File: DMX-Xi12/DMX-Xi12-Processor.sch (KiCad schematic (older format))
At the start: 3 parts, among them U1 LPC11U68JBD100E

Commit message: added output stage
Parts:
- added R? (x4): 10K, symbol R
- added SW?: DIPS_04, symbol DIPS_04
- added SW?: SW_PUSH, symbol SW_PUSH
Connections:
- net +5V: now also R?.1, R?.1, R?.1, R?.1
- net GND: now also SW?.1, SW?.2, SW?.2, SW?.3, SW?.4
- net at U1.1 (PIO2_23): now also R?.2, SW?.8
- net RX: now reaches U1.17 (PIO0_20)
- net RX_ENABLE: now reaches U1.33 (PIO0_21)
- net TX_ENABLE: now reaches U1.62 (PIO0_22)
- net at U1.75 (PIO2_20): now also R?.2, SW?.5
- net at U1.76 (PIO2_21): now also R?.2, SW?.6
- net at U1.77 (PIO2_22): now also R?.2, SW?.7
- net at C?.1, R?.2, U1.8 (RESET/PIO0_0): now also SW?.1
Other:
- moved on the sheet: R?
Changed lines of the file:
@@
 LIBS:valves
 LIBS:DMX-Xi12
+LIBS:dips-s
+LIBS:MyPower
 LIBS:DMX-Xi12-cache
 EELAYER 25 0
@@
 $Descr A4 11693 8268
 encoding utf-8
-Sheet 3 3
+Sheet 3 10
 Title "DMX-Xi12 Processor"
 Date ""
@@
 	1    0    0    -1
 $EndComp
-Wire Wire Line
-	5600 1750 5600 1700
-Wire Wire Line
-	5400 1700 6200 1700
-Wire Wire Line
-	5700 1700 5700 1750
-Wire Wire Line
-	5800 1700 5800 1750
-Connection ~ 5700 1700
-Wire Wire Line
-	5900 1700 5900 1750
-Connection ~ 5800 1700
-Wire Wire Line
-	6000 1700 6000 1750
-Connection ~ 5900 1700
-Wire Wire Line
-	6100 1700 6100 1750
-Connection ~ 6000 1700
-Wire Wire Line
-	6200 1700 6200 1750
-Connection ~ 6100 1700
-Wire Wire Line
-	6300 1400 6300 1750
-Wire Wire Line
-	6300 1700 6800 1700
-Wire Wire Line
-	6400 1700 6400 1750
-Wire Wire Line
-	6500 1700 6500 1750
-Connection ~ 6400 1700
-Wire Wire Line
-	6600 1700 6600 1750
-Connection ~ 6500 1700
-Wire Wire Line
-	6700 1700 6700 1750
-Connection ~ 6600 1700
-Wire Wire Line
-	6800 1700 6800 1750
-Connection ~ 6700 1700
-Wire Wire Line
-	5400 1400 5400 1750
-Connection ~ 5600 1700
-Wire Wire Line
-	5500 1750 5500 1600
-Wire Wire Line
-	5500 1600 6300 1600
-Connection ~ 6300 1700
 NoConn ~ 4900 1750
 $Comp
@@
 	1    0    0    -1
 $EndComp
-Connection ~ 6300 1600
 $Comp
 L GND #PWR?
@@
 	-1   0    0    1
 $EndComp
-Connection ~ 5400 1700
 $Comp
 L +5V #PWR?
 U 1 1 56AFFF45
-P 8100 2200
-F 0 "#PWR?" H 8100 2050 50  0001 C CNN
-F 1 "+5V" H 8100 2340 50  0000 C CNN
-F 2 "" H 8100 2200 50  0000 C CNN
-F 3 "" H 8100 2200 50  0000 C CNN
-	1    8100 2200
+P 8100 2050
+F 0 "#PWR?" H 8100 1900 50  0001 C CNN
+F 1 "+5V" H 8100 2190 50  0000 C CNN
+F 2 "" H 8100 2050 50  0000 C CNN
+F 3 "" H 8100 2050 50  0000 C CNN
+	1    8100 2050
 	1    0    0    -1
 $EndComp
@@
 L R R?
 U 1 1 56AFFF7D
-P 8100 2400
-F 0 "R?" V 8180 2400 50  0000 C CNN
-F 1 "4K7" V 8100 2400 50  0000 C CNN
-F 2 "" V 8030 2400 50  0000 C CNN
-F 3 "" H 8100 2400 50  0000 C CNN
-	1    8100 2400
+P 8100 2300
+F 0 "R?" V 8180 2300 50  0000 C CNN
+F 1 "4K7" V 8100 2300 50  0000 C CNN
+F 2 "" V 8030 2300 50  0000 C CNN
+F 3 "" H 8100 2300 50  0000 C CNN
+	1    8100 2300
 	1    0    0    -1
 $EndComp
@@
 	1    0    0    -1
 $EndComp
-Wire Wire Line
-	8100 2200 8100 2250
-Wire Wire Line
-	8100 2550 8100 2650
-Wire Wire Line
-	8100 2950 8100 3000
-Wire Wire Line
-	8100 2600 7850 2600
-Connection ~ 8100 2600
 Text HLabel 4500 5950 3    60   Output ~ 0
 CH3
@@
 Text HLabel 7400 5950 3    60   Output ~ 0
 CH32
+$Comp
+L DIPS_04 SW?
+U 1 1 56B54085
+P 3300 5250
+F 0 "SW?" V 3050 5250 60  0000 C CNN
+F 1 "DIPS_04" V 3550 5250 60  0000 C CNN
+F 2 "" H 3300 5250 60  0000 C CNN
+F 3 "" H 3300 5250 60  0000 C CNN
+	1    3300 5250
+	1    0    0    -1
+$EndComp
+$Comp
+L R R?
+U 1 1 56B54160
+P 3100 4300
+F 0 "R?" V 3180 4300 50  0000 C CNN
+F 1 "10K" V 3100 4300 50  0000 C CNN
+F 2 "" V 3030 4300 50  0000 C CNN
+F 3 "" H 3100 4300 50  0000 C CNN
+	1    3100 4300
+	1    0    0    -1
+$EndComp
+$Comp
+L R R?
+U 1 1 56B541AC
+P 3200 4300
+F 0 "R?" V 3280 4300 50  0000 C CNN
+F 1 "10K" V 3200 4300 50  0000 C CNN
+F 2 "" V 3130 4300 50  0000 C CNN
+F 3 "" H 3200 4300 50  0000 C CNN
+	1    3200 4300
+	1    0    0    -1
+$EndComp
+$Comp
+L R R?
+U 1 1 56B541F0
+P 3300 4300
+F 0 "R?" V 3380 4300 50  0000 C CNN
+F 1 "10K" V 3300 4300 50  0000 C CNN
+F 2 "" V 3230 4300 50  0000 C CNN
+F 3 "" H 3300 4300 50  0000 C CNN
+	1    3300 4300
+	1    0    0    -1
+$EndComp
+$Comp
+L R R?
+U 1 1 56B5422B
+P 3400 4300
+F 0 "R?" V 3480 4300 50  0000 C CNN
+F 1 "10K" V 3400 4300 50  0000 C CNN
+F 2 "" V 3330 4300 50  0000 C CNN
+F 3 "" H 3400 4300 50  0000 C CNN
+	1    3400 4300
+	1    0    0    -1
+$EndComp
+$Comp
+L +5V #PWR?
+U 1 1 56B54680
+P 3250 3900
+F 0 "#PWR?" H 3250 3750 50  0001 C CNN
+F 1 "+5V" H 3250 4040 50  0000 C CNN
+F 2 "" H 3250 3900 50  0000 C CNN
+F 3 "" H 3250 3900 50  0000 C CNN
+	1    3250 3900
+	1    0    0    -1
+$EndComp
+Text HLabel 8150 4600 2    60   Input ~ 0
+RX
+Text HLabel 8150 4700 2    60   Output ~ 0
+RX_ENABLE
+Text HLabel 8150 4800 2    60   Output ~ 0
+TX_ENABLE
+$Comp
+L GND #PWR?
+U 1 1 56B5699D
+P 3300 5750
+F 0 "#PWR?" H 3300 5500 50  0001 C CNN
+F 1 "GND" H 3300 5600 50  0000 C CNN
+F 2 "" H 3300 5750 50  0000 C CNN
+F 3 "" H 3300 5750 50  0000 C CNN
+	1    3300 5750
+	1    0    0    -1
+$EndComp
+$Comp
+L SW_PUSH SW?
+U 1 1 56B572F2
+P 8450 2900
+F 0 "SW?" H 8600 3010 50  0000 C CNN
+F 1 "SW_PUSH" H 8450 2820 50  0000 C CNN
+F 2 "" H 8450 2900 50  0000 C CNN
+F 3 "" H 8450 2900 50  0000 C CNN
+	1    8450 2900
+	0    1    1    0
+$EndComp
+Wire Wire Line
+	5600 1750 5600 1700
+Wire Wire Line
+	5400 1700 6200 1700
+Wire Wire Line
+	5700 1700 5700 1750
+Wire Wire Line
+	5800 1700 5800 1750
+Connection ~ 5700 1700
+Wire Wire Line
+	5900 1700 5900 1750
+Connection ~ 5800 1700
+Wire Wire Line
+	6000 1700 6000 1750
+Connection ~ 5900 1700
+Wire Wire Line
+	6100 1700 6100 1750
+Connection ~ 6000 1700
+Wire Wire Line
+	6200 1700 6200 1750
+Connection ~ 6100 1700
+Wire Wire Line
+	6300 1400 6300 1750
+Wire Wire Line
+	6300 1700 6800 1700
+Wire Wire Line
+	6400 1700 6400 1750
+Wire Wire Line
+	6500 1700 6500 1750
+Connection ~ 6400 1700
+Wire Wire Line
+	6600 1700 6600 1750
+Connection ~ 6500 1700
+Wire Wire Line
+	6700 1700 6700 1750
+Connection ~ 6600 1700
+Wire Wire Line
+	6800 1700 6800 1750
+Connection ~ 6700 1700
+Wire Wire Line
+	5400 1400 5400 1750
+Connection ~ 5600 1700
+Wire Wire Line
+	5500 1750 5500 1600
+Wire Wire Line
+	5500 1600 6300 1600
+Connection ~ 6300 1700
+Connection ~ 6300 1600
+Connection ~ 5400 1700
+Wire Wire Line
+	8100 2450 8100 2650
+Wire Wire Line
+	8100 2950 8100 3000
+Wire Wire Line
+	8100 2600 7850 2600
+Connection ~ 8100 2600
 Wire Wire Line
 	4300 5750 4300 5950
@@
 Wire Wire Line
 	7400 5750 7400 5950
+Wire Wire Line
+	3100 4450 3100 4900
+Wire Wire Line
+	3200 4450 3200 4800
+Wire Wire Line
+	3300 4450 3300 4700
+Wire Wire Line
+	3400 4600 3400 4450
+Wire Wire Line
+	3100 4150 3400 4150
+Connection ~ 3200 4150
+Connection ~ 3300 4150
+Wire Wire Line
+	3250 4150 3250 3900
+Connection ~ 3250 4150
+Wire Wire Line
+	8150 4600 7850 4600
+Wire Wire Line
+	7850 4700 8150 4700
+Wire Wire Line
+	8150 4800 7850 4800
+Wire Wire Line
+	3150 5050 3150 4900
+Connection ~ 3150 4900
+Wire Wire Line
+	3250 5050 3250 4800
+Connection ~ 3250 4800
+Wire Wire Line
+	3350 5050 3350 4700
+Connection ~ 3350 4700
+Wire Wire Line
+	3450 5050 3450 4600
+Connection ~ 3450 4600
+Wire Wire Line
+	3150 5450 3150 5550
+Wire Wire Line
+	3150 5550 3450 5550
+Wire Wire Line
+	3300 5550 3300 5750
+Wire Wire Line
+	3450 5550 3450 5450
+Connection ~ 3300 5550
+Wire Wire Line
+	3350 5450 3350 5550
+Connection ~ 3350 5550
+Wire Wire Line
+	3250 5450 3250 5550
+Connection ~ 3250 5550
+Wire Wire Line
+	3400 4600 3850 4600
+Wire Wire Line
+	3300 4700 3850 4700
+Wire Wire Line
+	3200 4800 3850 4800
+Wire Wire Line
+	3100 4900 3850 4900
+Wire Wire Line
+	8100 2050 8100 2150
+Wire Wire Line
+	8450 2600 8450 2500
+Wire Wire Line
+	8450 2500 8100 2500
+Connection ~ 8100 2500
+$Comp
+L GND #PWR?
+U 1 1 56B57753
+P 8450 3300
+F 0 "#PWR?" H 8450 3050 50  0001 C CNN
+F 1 "GND" H 8450 3150 50  0000 C CNN
+F 2 "" H 8450 3300 50  0000 C CNN
+F 3 "" H 8450 3300 50  0000 C CNN
+	1    8450 3300
+	1    0    0    -1
+$EndComp
+Wire Wire Line
+	8450 3300 8450 3200
 $EndSCHEMATC

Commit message: more schematic
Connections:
- net Zero_crossing: now reaches U1.57 (PIO2_19)
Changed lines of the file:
@@
 Wire Wire Line
 	8450 3300 8450 3200
+Text HLabel 3500 3600 0    60   Output ~ 0
+Zero_crossing
+Wire Wire Line
+	3500 3600 3600 3600
+Wire Wire Line
+	3600 3600 3600 4500
+Wire Wire Line
+	3600 4500 3850 4500
 $EndSCHEMATC

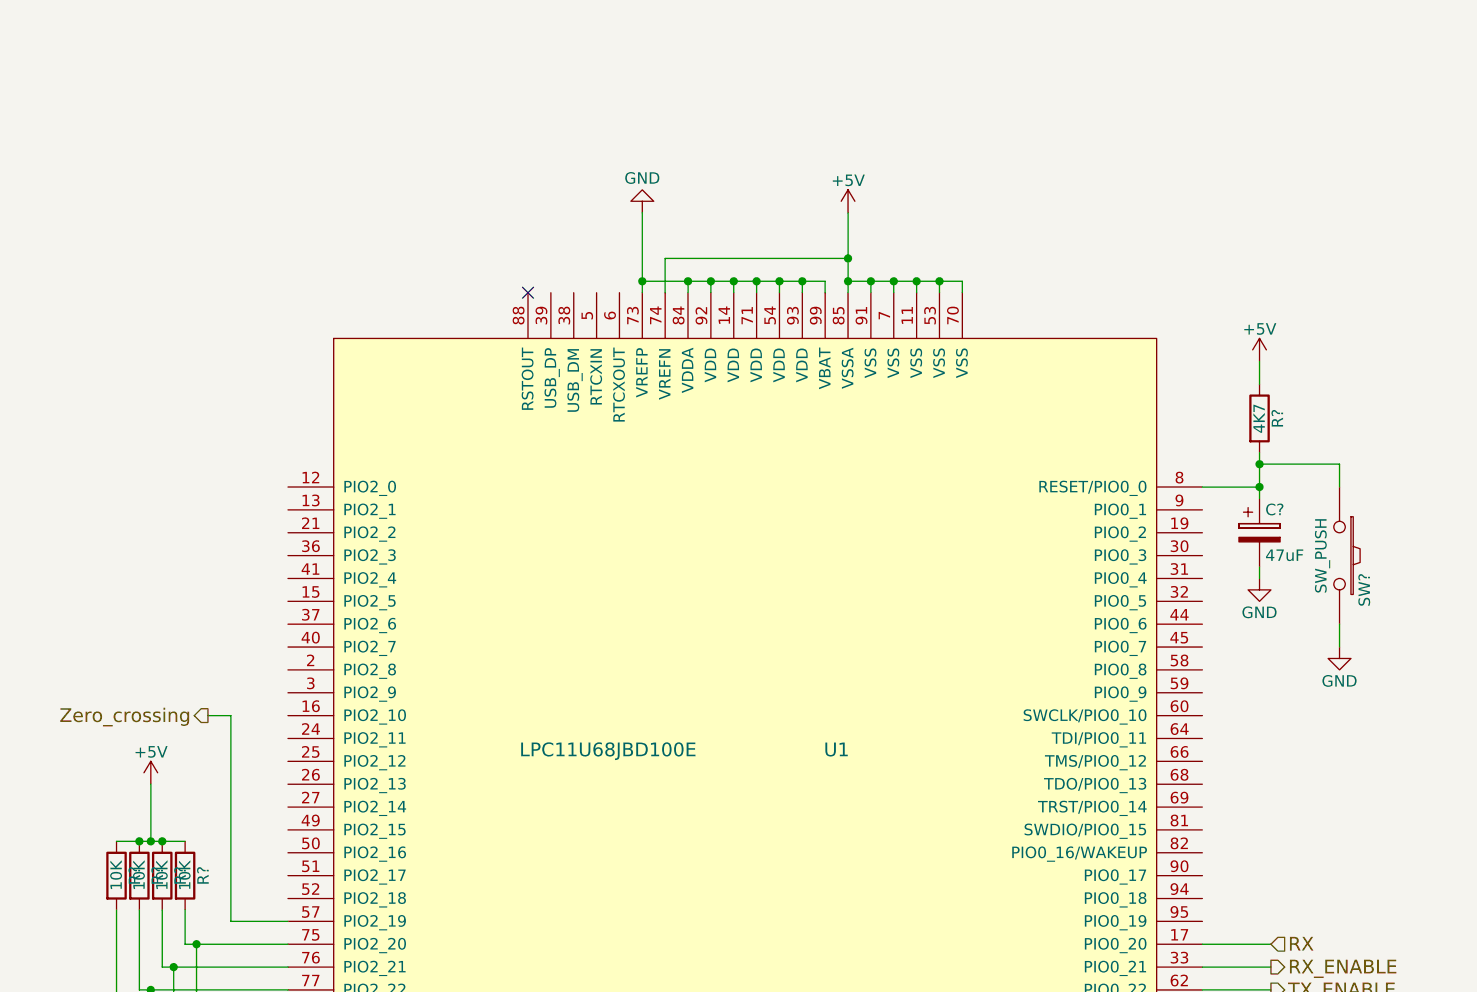
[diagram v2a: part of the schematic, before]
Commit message: changed processor to 3.3v and added programming
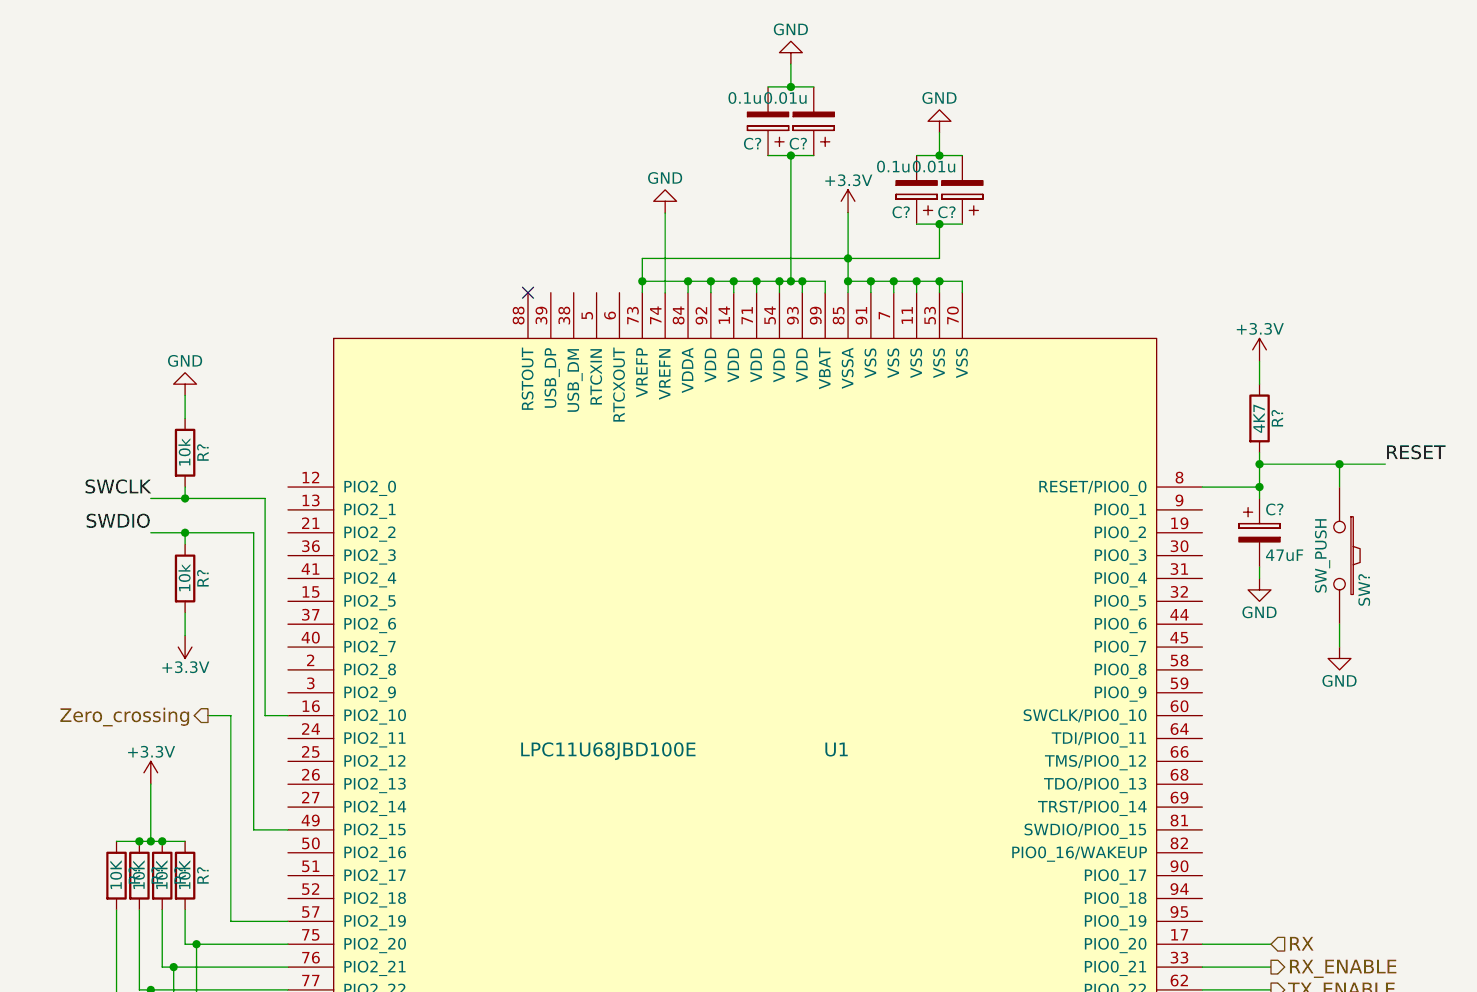
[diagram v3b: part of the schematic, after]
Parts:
- added C? (x2): 0.1u, symbol CP
- added C? (x2): 0.01u, symbol CP
- added R? (x2): 10k, symbol R
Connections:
- net GND: now also U1.74 (VREFN), C?.2, C?.2, C?.2, C?.2, R?.1; no longer U1.14 (VDD), U1.54 (VDD), U1.71 (VDD), U1.73 (VREFP), U1.84 (VDDA), U1.92 (VDD), U1.93 (VDD), U1.99 (VBAT)
- net SWCLK: now reaches U1.16 (PIO2_10)
- net SWCLK: now also R?.2
- net SWDIO: now reaches U1.49 (PIO2_15)
- net SWDIO: now also R?.1
- net RESET: now reaches C?.1, R?.2, SW?.1, U1.8 (RESET/PIO0_0)
- net +5V renamed +3V3
- net +3V3: now also U1.14 (VDD), U1.54 (VDD), U1.71 (VDD), U1.73 (VREFP), U1.84 (VDDA), U1.92 (VDD), U1.93 (VDD), U1.99 (VBAT), C?.1, C?.1, C?.1, C?.1, R?.2; no longer U1.74 (VREFN)
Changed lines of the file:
@@
 NoConn ~ 4900 1750
 $Comp
-L +5V #PWR?
-U 1 1 56AFFDE3
-P 6300 1400
-F 0 "#PWR?" H 6300 1250 50  0001 C CNN
-F 1 "+5V" H 6300 1540 50  0000 C CNN
-F 2 "" H 6300 1400 50  0000 C CNN
-F 3 "" H 6300 1400 50  0000 C CNN
-	1    6300 1400
-	1    0    0    -1
-$EndComp
-$Comp
 L GND #PWR?
 U 1 1 56AFFE1A
-P 5400 1400
-F 0 "#PWR?" H 5400 1150 50  0001 C CNN
-F 1 "GND" H 5400 1250 50  0000 C CNN
-F 2 "" H 5400 1400 50  0000 C CNN
-F 3 "" H 5400 1400 50  0000 C CNN
-	1    5400 1400
-	-1   0    0    1
-$EndComp
-$Comp
-L +5V #PWR?
-U 1 1 56AFFF45
-P 8100 2050
-F 0 "#PWR?" H 8100 1900 50  0001 C CNN
-F 1 "+5V" H 8100 2190 50  0000 C CNN
-F 2 "" H 8100 2050 50  0000 C CNN
-F 3 "" H 8100 2050 50  0000 C CNN
-	1    8100 2050
-	1    0    0    -1
+P 5500 1400
+F 0 "#PWR?" H 5500 1150 50  0001 C CNN
+F 1 "GND" H 5500 1250 50  0000 C CNN
+F 2 "" H 5500 1400 50  0000 C CNN
+F 3 "" H 5500 1400 50  0000 C CNN
+	1    5500 1400
+	-1   0    0    1
 $EndComp
 $Comp
@@
 	1    0    0    -1
 $EndComp
-$Comp
-L +5V #PWR?
-U 1 1 56B54680
-P 3250 3900
-F 0 "#PWR?" H 3250 3750 50  0001 C CNN
-F 1 "+5V" H 3250 4040 50  0000 C CNN
-F 2 "" H 3250 3900 50  0000 C CNN
-F 3 "" H 3250 3900 50  0000 C CNN
-	1    3250 3900
-	1    0    0    -1
-$EndComp
 Text HLabel 8150 4600 2    60   Input ~ 0
 RX
@@
 	6800 1700 6800 1750
 Connection ~ 6700 1700
-Wire Wire Line
-	5400 1400 5400 1750
 Connection ~ 5600 1700
 Wire Wire Line
-	5500 1750 5500 1600
-Wire Wire Line
-	5500 1600 6300 1600
+	5400 1600 6700 1600
 Connection ~ 6300 1700
 Connection ~ 6300 1600
@@
 	8450 2600 8450 2500
 Wire Wire Line
-	8450 2500 8100 2500
+	8100 2500 8650 2500
 Connection ~ 8100 2500
 $Comp
@@
 Wire Wire Line
 	3600 4500 3850 4500
+$Comp
+L CP C?
+U 1 1 56CD31E0
+P 5950 1000
+F 0 "C?" H 5975 1100 50  0000 L CNN
+F 1 "0.1u" H 5975 900 50  0000 L CNN
+F 2 "" H 5988 850 50  0000 C CNN
+F 3 "" H 5950 1000 50  0000 C CNN
+	1    5950 1000
+	-1   0    0    1
+$EndComp
+$Comp
+L CP C?
+U 1 1 56CD3257
+P 6150 1000
+F 0 "C?" H 6175 1100 50  0000 L CNN
+F 1 "0.01u" H 6175 900 50  0000 L CNN
+F 2 "" H 6188 850 50  0000 C CNN
+F 3 "" H 6150 1000 50  0000 C CNN
+	1    6150 1000
+	-1   0    0    1
+$EndComp
+Wire Wire Line
+	5950 1150 6150 1150
+Wire Wire Line
+	5950 850  6150 850
+$Comp
+L GND #PWR?
+U 1 1 56CD344B
+P 6050 750
+F 0 "#PWR?" H 6050 500 50  0001 C CNN
+F 1 "GND" H 6050 600 50  0000 C CNN
+F 2 "" H 6050 750 50  0000 C CNN
+F 3 "" H 6050 750 50  0000 C CNN
+	1    6050 750
+	-1   0    0    1
+$EndComp
+Wire Wire Line
+	6050 750  6050 850
+Connection ~ 6050 850
+Wire Wire Line
+	6050 1150 6050 1700
+Connection ~ 6050 1700
+Connection ~ 6050 1150
+Wire Wire Line
+	5400 1600 5400 1750
+Wire Wire Line
+	5500 1400 5500 1750
+$Comp
+L CP C?
+U 1 1 56CD39E9
+P 6600 1300
+F 0 "C?" H 6625 1400 50  0000 L CNN
+F 1 "0.1u" H 6625 1200 50  0000 L CNN
+F 2 "" H 6638 1150 50  0000 C CNN
+F 3 "" H 6600 1300 50  0000 C CNN
+	1    6600 1300
+	-1   0    0    1
+$EndComp
+$Comp
+L CP C?
+U 1 1 56CD39EF
+P 6800 1300
+F 0 "C?" H 6825 1400 50  0000 L CNN
+F 1 "0.01u" H 6825 1200 50  0000 L CNN
+F 2 "" H 6838 1150 50  0000 C CNN
+F 3 "" H 6800 1300 50  0000 C CNN
+	1    6800 1300
+	-1   0    0    1
+$EndComp
+Wire Wire Line
+	6600 1450 6800 1450
+Wire Wire Line
+	6600 1150 6800 1150
+$Comp
+L GND #PWR?
+U 1 1 56CD39F7
+P 6700 1050
+F 0 "#PWR?" H 6700 800 50  0001 C CNN
+F 1 "GND" H 6700 900 50  0000 C CNN
+F 2 "" H 6700 1050 50  0000 C CNN
+F 3 "" H 6700 1050 50  0000 C CNN
+	1    6700 1050
+	-1   0    0    1
+$EndComp
+Wire Wire Line
+	6700 1050 6700 1150
+Connection ~ 6700 1150
+Connection ~ 6700 1450
+Wire Wire Line
+	6700 1600 6700 1450
+Text Label 3250 2800 2    60   ~ 0
+SWDIO
+Text Label 3250 2650 2    60   ~ 0
+SWCLK
+Wire Wire Line
+	3250 2800 3700 2800
+Wire Wire Line
+	3700 2800 3700 4100
+Wire Wire Line
+	3700 4100 3850 4100
+Wire Wire Line
+	3250 2650 3750 2650
+Wire Wire Line
+	3750 2650 3750 3600
+Wire Wire Line
+	3750 3600 3850 3600
+$Comp
+L R R?
+U 1 1 56CD42DA
+P 3400 2450
+F 0 "R?" V 3480 2450 50  0000 C CNN
+F 1 "10k" V 3400 2450 50  0000 C CNN
+F 2 "" V 3330 2450 50  0000 C CNN
+F 3 "" H 3400 2450 50  0000 C CNN
+	1    3400 2450
+	1    0    0    -1
+$EndComp
+$Comp
+L R R?
+U 1 1 56CD433D
+P 3400 3000
+F 0 "R?" V 3480 3000 50  0000 C CNN
+F 1 "10k" V 3400 3000 50  0000 C CNN
+F 2 "" V 3330 3000 50  0000 C CNN
+F 3 "" H 3400 3000 50  0000 C CNN
+	1    3400 3000
+	1    0    0    -1
+$EndComp
+Wire Wire Line
+	3400 2850 3400 2800
+Connection ~ 3400 2800
+Wire Wire Line
+	3400 2650 3400 2600
+Connection ~ 3400 2650
+$Comp
+L GND #PWR?
+U 1 1 56CD4612
+P 3400 2200
+F 0 "#PWR?" H 3400 1950 50  0001 C CNN
+F 1 "GND" H 3400 2050 50  0000 C CNN
+F 2 "" H 3400 2200 50  0000 C CNN
+F 3 "" H 3400 2200 50  0000 C CNN
+	1    3400 2200
+	-1   0    0    1
+$EndComp
+Wire Wire Line
+	3400 2200 3400 2300
+Wire Wire Line
+	3400 3150 3400 3250
+Text Label 8650 2500 0    60   ~ 0
+RESET
+Connection ~ 8450 2500
+$Comp
+L +3.3V #PWR?
+U 1 1 56CD4DFF
+P 6300 1400
+F 0 "#PWR?" H 6300 1250 50  0001 C CNN
+F 1 "+3.3V" H 6300 1540 50  0000 C CNN
+F 2 "" H 6300 1400 50  0000 C CNN
+F 3 "" H 6300 1400 50  0000 C CNN
+	1    6300 1400
+	1    0    0    -1
+$EndComp
+$Comp
+L +3.3V #PWR?
+U 1 1 56CD4EF5
+P 8100 2050
+F 0 "#PWR?" H 8100 1900 50  0001 C CNN
+F 1 "+3.3V" H 8100 2190 50  0000 C CNN
+F 2 "" H 8100 2050 50  0000 C CNN
+F 3 "" H 8100 2050 50  0000 C CNN
+	1    8100 2050
+	1    0    0    -1
+$EndComp
+$Comp
+L +3.3V #PWR?
+U 1 1 56CD53C9
+P 3250 3900
+F 0 "#PWR?" H 3250 3750 50  0001 C CNN
+F 1 "+3.3V" H 3250 4040 50  0000 C CNN
+F 2 "" H 3250 3900 50  0000 C CNN
+F 3 "" H 3250 3900 50  0000 C CNN
+	1    3250 3900
+	1    0    0    -1
+$EndComp
+$Comp
+L +3.3V #PWR?
+U 1 1 56CD5492
+P 3400 3250
+F 0 "#PWR?" H 3400 3100 50  0001 C CNN
+F 1 "+3.3V" H 3400 3390 50  0000 C CNN
+F 2 "" H 3400 3250 50  0000 C CNN
+F 3 "" H 3400 3250 50  0000 C CNN
+	1    3400 3250
+	-1   0    0    1
+$EndComp
 $EndSCHEMATC

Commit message: made dlaw changes etc
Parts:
- removed C?: 0.1u, symbol CP
- removed C?: 0.01u, symbol CP
- removed R? (x4): 10K, symbol R
- removed R? (x2): 10k, symbol R
- added C? (x2): 18/39pf, symbol C
- added C? (x5): 0.1u, symbol CP
- added C? (x5): 0.01u, symbol CP
- added Con?: Cortex-10-SWD, symbol Cortex-10-SWD
- added P?: USB_B, symbol USB_B
- added R? (x2): 10, symbol R
- added R? (x2): 10k, symbol R
- added SW?: SW_PUSH, symbol SW_PUSH
- added Y?: 12MHz 10/20pf, symbol Crystal
- C?: value 47uF -> 4.7uF
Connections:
- net +3V3: now also U1.30 (PIO0_3), C?.1, C?.1, C?.1, C?.1, C?.1, C?.1, C?.1, C?.1, C?.1, C?.1, Con?.1 (VCC), R?.1; no longer U1.11 (VSS), U1.53 (VSS), U1.7 (VSS), U1.70 (VSS), U1.85 (VSSA), U1.91 (VSS)
- net GND: now also U1.11 (VSS), U1.5 (RTCXIN), U1.53 (VSS), U1.7 (VSS), U1.70 (VSS), U1.85 (VSSA), U1.91 (VSS), C?.2, C?.2, C?.2, C?.2, C?.2, C?.2, C?.2, C?.2, C?.2, C?.2, C?.2, C?.2, Con?.3 (GND), Con?.5 (GND), Con?.9 (GNDDetect), P?.4 (GND), P?.5 (shield), R?.2, SW?.2
- net RESET: now also Con?.10 (nRESET)
- net at U1.1 (PIO2_23): now also SW?.5; no longer SW?.8
- net at U1.12 (PIO2_0): now also C?.1, Y?.1
- net at U1.13 (PIO2_1): now also C?.1, Y?.2
- net at U1.38 (USB_DM): now also R?.2
- net at U1.39 (USB_DP): now also R?.2
- net Zero_crossingB: now reaches U1.52 (PIO2_18)
- net at U1.60 (SWCLK/PIO0_10): now also Con?.4 (SWDCLK/TCK)
- net at U1.75 (PIO2_20): now also SW?.8; no longer SW?.5
- net at U1.76 (PIO2_21): now also SW?.7; no longer SW?.6
- net at U1.77 (PIO2_22): now also SW?.6; no longer SW?.7
- net at U1.82 (PIO0_16/WAKEUP): now also Con?.2 (SWDIO/TMS), R?.2
- net at U1.9 (PIO0_1): now also SW?.1
- net SWCLK: no longer names the net of U1.16 (PIO2_10)
- net SWDIO: no longer names the net of U1.49 (PIO2_15)
- net Zero_crossing renamed Zero_crossingA
- new net: P?.2 (D-), R?.1
- new net: P?.3 (D+), R?.1
- no-connect marks 1 -> 6
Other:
- moved on the sheet: C?, R?, SW?, U1
